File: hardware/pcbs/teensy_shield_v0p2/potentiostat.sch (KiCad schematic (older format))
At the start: 141 parts, among them K1 CONN_3, P1 CONN_2, P10 CONN_2, P11 CONN_2, P12 CONN_2, P13 CONN_5X2, P14 CONN_5X2, P15 CONN_2X2, P16 CONN_2X2, P17 CONN_2, P18 CONN_2, P19 CONN_2, P2 CONN_2, P20 CONN_2, P21 CONN_2, P3 CONN_2, P4 CONN_2, P5 CONN_2, P6 CONN_2, P7 CONN_2, P8 CONN_2, P9 CONN_2, U1 ZXRE060, U10 OPA227, U11 OP07, U12 LT1995, U13 ADG44X, U2 TEENSY3.1, U3 MAX6176AASA+, U4 LT1995, U5 AD8250, U6 MEA1D05XXSC, U7 OPA129, U8 OPA129, U9 ADG44X

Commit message: Worked on version 0.2 of teensy shield.
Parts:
- removed R?: 20k, symbol Device:R
- removed R? (x2): 10k, symbol Device:R
- removed R?: 50k, symbol Device:R
- removed R?: 120k, symbol Device:R
- removed R?: 36k, symbol Device:R
- removed U?: REF3312, symbol REF3312:REF3312
- added D?: BAS07-04, ~, symbol potentiostat-rescue:BAS07-04
- added R? (x2): 12k, symbol Device:R
- added R?: 100k, symbol Device:R
- added R? (x3): 20k, symbol Device:R
- added R?: 1k, symbol Device:R
- added R?: 100, symbol Device:R
- added U?: REF33XX, symbol REF33XX:REF33XX
- R?: value R -> 20k
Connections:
- net labels added: REF_3V, REF_NEG_0V6, REF_NEG_10V
- net labels removed: REF_1V25
- wire segments 702 -> 719
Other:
- note added: "-0.6V ref. voltage test point"
- note added: "3V Reference Voltage\n\nLCSC#: C140329\nREF3330AIDBZR"
- note added: "Notes:\n\n1.) Don't forget the bypass capacitors!!!\n2.) Maybe change +/-12V DC-DC converter to \n +/-15V DC-DC converter to give op07's more head room."
- note removed: "1.25V Reference Voltage\n\nLCSC#: C183104"
- note removed: "Don't forget the bypass capacitors!!!"
- note removed: "This will be inverting adder ...."
- moved on the sheet: C?, P10, P6, P7, P8, P9, R?, U?

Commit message: Worked on version 0.2 of teensy pcb.
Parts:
- added C? (x20): 0.1uF, symbol Device:C
- added C?: 3.3nF, symbol Device:C
- added C?: 12nF, symbol Device:C
- added C? (x4): 56nF, symbol Device:C
- added D?: BAS07-04, ~, symbol potentiostat-rescue:BAS07-04
- added K1: Conn_01x03, symbol Connector_Generic:Conn_01x03
- added P1, P2, P3: Conn_01x02, symbol Connector_Generic:Conn_01x02
- added R?: 300k, symbol Device:R
- added R?: 300, symbol Device:R
- added R?: 30k, symbol Device:R
- added R?: 3k, symbol Device:R
- added R? (x2): 20k, symbol Device:R
- added R? (x2): 12k, symbol Device:R
- added R?: 1k, symbol Device:R
- added R?: 100, symbol Device:R
- added R?: 10k, symbol Device:R
- added U? (x3): TL072, symbol Amplifier_Operational:TL072
- added U? (x15): DG411xY, Package_SO:SOIC-16_3.9x9.9mm_P1.27mm, symbol Analog_Switch:DG411xY
- added U?: 74HC138, symbol 74HC138:74HC138
- added U? (x2): OP07, symbol Amplifier_Operational:OP07
- U2: symbol potentiostat-rescue:TEENSY3.1 -> teensy3:TEENSY3.1
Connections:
- net labels added: CTR_ELECT_OUT, D3, D4, REF_ELECT_BIP, REF_ELECT_OUT, REF_GAIN_A0, REF_GAIN_A1, SW_CTR_ELECT, SW_REF_ELECT, SW_TIA_GAIN_1, SW_TIA_GAIN_2, SW_TIA_GAIN_3, SW_TIA_GAIN_4, SW_WRK_ELECT, TIA_GAIN_A0, TIA_GAIN_A1, WRK_ELECT_OUT
- net labels removed: DAC_GAIN_B0, DAC_GAIN_B1, REF_NEG_10V, RX, TX
- wire segments 719 -> 960
- no-connect marks 56 -> 68
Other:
- note added: "Notes:\n\n1.) Don't forget the bypass capacitors!!!\n2.) Maybe change DC converter from +/-12V to +/-15V \n3.) Add switch to working electrode ( and counter and reference?)\n4.) Add low pass filters to inputs (DAC) and outputs (ADC)\n"
- note added: "OP07\nLCSC# C7433"
- note added: "Scale bipolar DAC (DAC_BIP) by gain N=1,2,5, or 10 to get DAC_BIP_NX. \nGain is selected using DAC_GAIN_A0 and DAC_GAIN_A1"
- note added: "Shift and scales unipolar DAC (DAC_UNI) from [0V,1.2V] \nrange to bipolar DAC (DAC_BIP) in [-1V,1V] range. \n"
- note added: "TL072 power\n\nLCSC# C6961"
- note added: "gain select demux\nLCSC#: C5602"
- note added: "op amp decoupling capacitors"
- note added: "scale TIA signal by 2x"
- note added: "scale buffered reference electrode voltage\n according to gain setting"
- note added: "shift TIA signal to 0-1.2V range"
- note added: "switch power\nLCSC#: C17218"
- note added: "transimpedance amplifier with selectable gain using kelvin switching\nsee http://www.analog.com/library/analogdialogue/archives/47-05/pgtia.html\n\nSet gains so that output voltage range is -0.6V to 0.6V. \nInput current ranges (+/-) 1uA, 10uA, 100uA, 1000uA \n"
- note removed: "LCSC# C7433"
- note removed: "Notes:\n\n1.) Don't forget the bypass capacitors!!!\n2.) Maybe change +/-12V DC-DC converter to \n +/-15V DC-DC converter to give op07's more head room."
- moved on the sheet: C?, D?, K1, P1, P10, P2, P3, P6, P7, P8, P9, R?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

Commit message: Worked on revision 0.2 of teensy pcb.
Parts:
- removed C1, C30, C37, C39, C5: 10nF, ~, symbol potentiostat-rescue:C
- removed C10, C11, C12, C13, C14, C15, C17, C2, C23, C24, C25, C27, C28, C33, C34, C35, C6: 0.1uF, ~, symbol potentiostat-rescue:C
- removed C16, C18, C26, C29, C31, C36, C4, C8: 10uF, ~, symbol potentiostat-rescue:CP1
- removed C19, C20, C21, C22: 56nF, ~, symbol potentiostat-rescue:C
- removed C3, C32, C7: 4.7uF, ~, symbol potentiostat-rescue:CP1
- removed C38: 4.7uf, ~, symbol potentiostat-rescue:CP1
- removed C9: 1uF, ~, symbol potentiostat-rescue:C
- removed D1, D2: BAS07-04, ~, symbol potentiostat-rescue:BAS07-04
- removed K1: CONN_3, symbol potentiostat-rescue:CONN_3
- removed P1, P10, P11, P12, P17, P18, P19, P2, P20, P21, P3, P4, P5, P6, P7, P8, P9: CONN_2, symbol potentiostat-rescue:CONN_2
- removed P13, P14: CONN_5X2, symbol potentiostat-rescue:CONN_5X2
- removed P15, P16: CONN_2X2, symbol potentiostat-rescue:CONN_2X2
- removed R1, R15, R18: 1k, ~, symbol potentiostat-rescue:R
- removed R10, R11, R9: 50k, ~, symbol potentiostat-rescue:R
- removed R12, R13: 3k, ~, symbol potentiostat-rescue:R
- removed R14, R16: 4.7k, ~, symbol potentiostat-rescue:R
- removed R17, R19: 100, ~, symbol potentiostat-rescue:R
- removed R2, R3: 10k, ~, symbol potentiostat-rescue:R
- removed R4: 191, ~, symbol potentiostat-rescue:R
- removed R5: 600, ~, symbol potentiostat-rescue:R
- removed R6: 6k, ~, symbol potentiostat-rescue:R
- removed R7: 60k, ~, symbol potentiostat-rescue:R
- removed R8: 600k, ~, symbol potentiostat-rescue:R
- removed U1: ZXRE060, ~, symbol potentiostat-rescue:ZXRE060
- removed U10: OPA227, ~, symbol potentiostat-rescue:OPA227
- removed U11: OP07, ~, symbol potentiostat-rescue:OP07
- removed U12, U4: LT1995, ~, symbol potentiostat-rescue:LT1995
- removed U13, U9: ADG44X, symbol potentiostat-rescue:ADG44X
- removed U3: MAX6176AASA+, ~, symbol potentiostat-rescue:MAX6176AASA+
- removed U5: AD8250, ~, symbol potentiostat-rescue:AD8250
- removed U7, U8: OPA129, ~, symbol potentiostat-rescue:OPA129
- added C? (x16): 0.1uF, symbol Device:C
- added C? (x4): 1uF, symbol Device:C
- added C? (x3): 2.2uF, symbol Device:C
- added P10, P11, P12, P17, P18, P19, P20, P21, P4, P5, P6, P7, P8, P9, P?: Conn_01x02, symbol Connector_Generic:Conn_01x02
- added P13, P14: Conn_02x05_Odd_Even, symbol Connector_Generic:Conn_02x05_Odd_Even
- added P15, P16: Conn_02x02_Odd_Even, symbol Connector_Generic:Conn_02x02_Odd_Even
- added R? (x2): 4.7k, symbol Device:R
- U6: symbol potentiostat-rescue:MEA1D05XXSC -> mea1d05xxsc:MEA1D05XXSC
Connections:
- net labels removed: REF_10V, TIA_SW1_IN1, TIA_SW1_IN2, TIA_SW1_IN3, TIA_SW1_IN4, TIA_SW2_IN1, TIA_SW2_IN2, TIA_SW2_IN3, TIA_SW2_IN4
- wire segments 960 -> 650
- no-connect marks 68 -> 51
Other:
- note added: "0.6V reference test points"
- note added: "12V power decoupling caps"
- note added: "3V reference \n\nLCSC#: C140329\nREF3330AIDBZR"
- note added: "DAC test points"
- note added: "Reference electrode test points"
- note added: "TL072 power\nLCSC# C6961"
- note added: "bipolor/unipolar transimpedance \namplifier output test points"
- note added: "demux decoupling"
- note added: "demux decoupling capacitors"
- note added: "op amp decoupling"
- note added: "switch decoupling"
- note removed: "-0.6V ref. voltage test point"
- note removed: "0.6V ref. voltage test point"
- note removed: "10V Reference voltage."
- note removed: "10V ref. voltage test point"
- note removed: "3V Reference Voltage\n\nLCSC#: C140329\nREF3330AIDBZR"
- note removed: "Amplifier Gain=1.67"
- note removed: "DAC_GAIN_A0 and DAC_GAIN_A1."
- note removed: "Differential Amplifier - shifts and scales +/- 10V REF_ELECT_BUF into 0-1.2V range for analog input."
- note removed: "For switch arrangement see http://www.analog.com/library/analogdialogue/archives/47-05/pgtia.html\n\nSet gains so that output voltage range is -0.6V to 0.6V. \n\nInput current ranges (+/-) 1uA, 10uA, 100uA, 1000uA \n\nC values - may need tobe refined"
- note removed: "NX scaled DAC test point"
- note removed: "Scale bipolar DAC (DAC_BIP) by gain N=1,2,5, or 10 to get DAC_BIP_NX. Gain is selected using"
- note removed: "Shift and scales unipolar DAC (DAC_UNI) from [0V,1.2V] range to bipolar DAC (DAC_BIP) in [-1V,1V] range. \n"
- note removed: "TL072 power\n\nLCSC# C6961"
- note removed: "Transimpedance Amplifier"
- note removed: "Use ADG441"
- note removed: "Voltage Reference, 0.6V, Tol. 0.5%. Used in when shifting DAC_UNI to DAC_BIP."
- note removed: "bipolor/unipolar transimpedance \namplifier output test poinsts"
- note removed: "buffered ref. electrode test point"
- note removed: "op amp decoupling capacitors"
- note removed: "unipolar ref. electrode test point"
- note removed: "unipolar/bipolar DAC test points"
- moved on the sheet: C?, D?, R?, U2, U6, U?

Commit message: Finished initial draft of version 0.2 of teensy pcb.
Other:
- note added: "3V reference \nLCSC#: C140329\nREF3330AIDBZR"
- note added: "Analog Ouput Subsystem"
- note added: "Control & Reference Subsystem"
- note added: "Electrode Connection Subsystem"
- note added: "Expansion Headers"
- note added: "Op Amp Power Rails"
- note added: "Reference voltages"
- note added: "Switch and demux decoupling"
- note added: "Transimpedance Subsystem"
- note added: "electrode connections"
- note added: "inverts -0.6V reference to \ncreate 0.6V reference"
- note added: "power decoupling"
- note added: "scales 3V reference to \ncreate -0.6V reference"
- note added: "switches for connecting/disconnecting electrodes"
- note removed: "3V reference \n\nLCSC#: C140329\nREF3330AIDBZR"
- note removed: "Electrode Connectors"
- moved on the sheet: C?, D?, R?, U6, U?

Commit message: Worked on teensy shield version 0.2. Ported footprints from .mod to .kicad_mod.   Finished initial footprint assignments.
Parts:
- C1, C10, C11, C12, C13, C14, C15, C16, C17, C18, C19, C2, C20, C21, C22, C23, C24, C25, C26, C27, C28, C29, C3, C30, C31, C32, C33, C34, C35, C36, C37, C38, C39, C4, C40, C41, C42, C43, C44, C45, C46, C47, C48, C49, C5, C50, C51, C52, C6, C7, C8, C9: renamed from C?; footprint (none) -> Capacitor_SMD:C_0603_1608Metric
- D1, D2: renamed from D?; footprint ~ -> Package_TO_SOT_SMD:SOT-23
- K1: footprint (none) -> pin_array:PIN_ARRAY_3X1
- P1, P10, P11, P12, P17, P18, P19, P2, P20, P21, P3, P4, P5, P6, P7, P8, P9: footprint (none) -> pin_array:PIN_ARRAY_2X1
- P13, P14: footprint (none) -> 5x2_shrd_header:5X2_SHRD_HEADER
- P15, P16: footprint (none) -> pin_array:PIN_ARRAY_2X2
- P22: renamed from P?; footprint (none) -> pin_array:PIN_ARRAY_2X1
- R1, R10, R11, R12, R13, R14, R15, R16, R17, R18, R19, R2, R20, R21, R22, R23, R24, R25, R26, R27, R28, R29, R3, R30, R31, R32, R33, R34, R35, R36, R37, R38, R4, R5, R6, R7, R8, R9: renamed from R?; footprint (none) -> Resistor_SMD:R_0603_1608Metric
- U1, U19, U21: renamed from U?; footprint (none) -> Package_SO:SOIC-16_3.9x9.9mm_P1.27mm
- U10: renamed from U?; footprint (none) -> Package_TO_SOT_SMD:SOT-23
- U11, U12, U13, U14, U15, U16, U17, U18, U20, U9: renamed from U?; footprint (none) -> Package_SO:SOIC-8_3.9x4.9mm_P1.27mm
- U2: footprint ~ -> teensy3x:TEENSY3X
- U6: footprint ~ -> MEA1:MEA1
- gave numbers to parts that had none: 5
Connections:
- net labels added: +15V, -15V
- net labels removed: +12V, -12V
- wire segments 650 -> 652
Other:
- note added: "Notes:\n\n1.) Don't forget the bypass capacitors!!!\n2.) Maybe change DC converter from +/-15V to +/-15V \n3.) Add switch to working electrode ( and counter and reference?)\n4.) Add low pass filters to inputs (DAC) and outputs (ADC)\n"
- note removed: "Notes:\n\n1.) Don't forget the bypass capacitors!!!\n2.) Maybe change DC converter from +/-12V to +/-15V \n3.) Add switch to working electrode ( and counter and reference?)\n4.) Add low pass filters to inputs (DAC) and outputs (ADC)\n"

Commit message: Work on layout of teensy pcb version 0.2
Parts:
- added C53, C54, C55: 0.1uF, Capacitor_SMD:C_0603_1608Metric, symbol Device:C
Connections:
- wire segments 652 -> 658
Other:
- note added: "U18, U20 op amp decoupling"
- note added: "U9 op amp decoupling"
- moved on the sheet: C46, C49
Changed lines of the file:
@@
 Text Notes 8750 9275 0    60   ~ 0
 DAC test points
-Text Notes 26325 5800 0    60   ~ 0
+Text Notes 27500 5825 0    60   ~ 0
 bipolor/unipolar transimpedance \namplifier output test points
 Text Label 8200 11700 2    60   ~ 0
@@
 	27900 1325 27900 1475
 Text Notes 26575 2425 0    60   ~ 0
-op amp decoupling
+U18, U20 op amp decoupling
 $Comp
 L Device:C C34
@@
 	25575 1275 25575 1425
 Text Notes 24875 2425 0    60   ~ 0
-op amp decoupling
+U9 op amp decoupling
 $Comp
 L Device:C C10
@@
 L Device:C C46
 U 1 1 605E8CC1
-P 26950 3300
-F 0 "C46" H 27065 3346 50  0000 L CNN
-F 1 "0.1uF" H 27065 3255 50  0000 L CNN
-F 2 "Capacitor_SMD:C_0603_1608Metric" H 26988 3150 50  0001 C CNN
-F 3 "~" H 26950 3300 50  0001 C CNN
-	1    26950 3300
+P 25850 5150
+F 0 "C46" H 25965 5196 50  0000 L CNN
+F 1 "0.1uF" H 25965 5105 50  0000 L CNN
+F 2 "Capacitor_SMD:C_0603_1608Metric" H 25888 5000 50  0001 C CNN
+F 3 "~" H 25850 5150 50  0001 C CNN
+	1    25850 5150
 	1    0    0    -1
 $EndComp
@@
 L Device:C C49
 U 1 1 605E95B1
-P 27450 3300
-F 0 "C49" H 27565 3346 50  0000 L CNN
-F 1 "1uF" H 27565 3255 50  0000 L CNN
-F 2 "Capacitor_SMD:C_0603_1608Metric" H 27488 3150 50  0001 C CNN
-F 3 "~" H 27450 3300 50  0001 C CNN
-	1    27450 3300
+P 26350 5150
+F 0 "C49" H 26465 5196 50  0000 L CNN
+F 1 "1uF" H 26465 5105 50  0000 L CNN
+F 2 "Capacitor_SMD:C_0603_1608Metric" H 26388 5000 50  0001 C CNN
+F 3 "~" H 26350 5150 50  0001 C CNN
+	1    26350 5150
 	1    0    0    -1
 $EndComp
-Text Label 27450 3000 1    60   ~ 0
+Text Label 26350 4850 1    60   ~ 0
 3V3
-Text Label 26950 3000 1    60   ~ 0
+Text Label 25850 4850 1    60   ~ 0
 3V3
 Wire Wire Line
-	27450 3450 27450 3650
-Text Label 27450 3650 3    60   ~ 0
+	26350 5300 26350 5500
+Text Label 26350 5500 3    60   ~ 0
 GND
 Wire Wire Line
-	26950 3450 26950 3650
-Text Label 26950 3650 3    60   ~ 0
+	25850 5300 25850 5500
+Text Label 25850 5500 3    60   ~ 0
 GND
 Wire Wire Line
-	26950 3000 26950 3150
+	25850 4850 25850 5000
 Wire Wire Line
-	27450 3000 27450 3150
+	26350 4850 26350 5000
 $Comp
 L Device:C C13
@@
 Text Notes 24950 10925 0    60   ~ 0
 switch decoupling
-Text Notes 26775 4100 0    50   ~ 0
+Text Notes 25675 5950 0    50   ~ 0
 demux decoupling capacitors
 $Comp
@@
 Wire Wire Line
 	25525 3000 25525 3150
-Text Notes 25125 4100 0    60   ~ 0
+Text Notes 26175 4150 0    60   ~ 0
 switch decoupling
 $Comp
@@
 L Connector_Generic:Conn_01x02 P17
 U 1 1 67FDB608
-P 27400 4725
-F 0 "P17" H 27480 4717 50  0000 L CNN
-F 1 "Conn_01x02" H 27480 4626 50  0000 L CNN
-F 2 "pin_array:PIN_ARRAY_2X1" H 27400 4725 50  0001 C CNN
-F 3 "~" H 27400 4725 50  0001 C CNN
-	1    27400 4725
+P 28575 4750
+F 0 "P17" H 28655 4742 50  0000 L CNN
+F 1 "Conn_01x02" H 28655 4651 50  0000 L CNN
+F 2 "pin_array:PIN_ARRAY_2X1" H 28575 4750 50  0001 C CNN
+F 3 "~" H 28575 4750 50  0001 C CNN
+	1    28575 4750
 	1    0    0    -1
 $EndComp
@@
 L Connector_Generic:Conn_01x02 P18
 U 1 1 67FDF739
-P 27400 5325
-F 0 "P18" H 27480 5317 50  0000 L CNN
-F 1 "Conn_01x02" H 27480 5226 50  0000 L CNN
-F 2 "pin_array:PIN_ARRAY_2X1" H 27400 5325 50  0001 C CNN
-F 3 "~" H 27400 5325 50  0001 C CNN
-	1    27400 5325
+P 28575 5350
+F 0 "P18" H 28655 5342 50  0000 L CNN
+F 1 "Conn_01x02" H 28655 5251 50  0000 L CNN
+F 2 "pin_array:PIN_ARRAY_2X1" H 28575 5350 50  0001 C CNN
+F 3 "~" H 28575 5350 50  0001 C CNN
+	1    28575 5350
 	1    0    0    -1
 $EndComp
 Wire Wire Line
-	27200 4725 27100 4725
+	28375 4750 28275 4750
 Wire Wire Line
-	27100 4725 27100 4775
+	28275 4750 28275 4800
 Wire Wire Line
-	27100 4825 27200 4825
+	28275 4850 28375 4850
 Wire Wire Line
-	27200 5325 27100 5325
+	28375 5350 28275 5350
 Wire Wire Line
-	27100 5325 27100 5375
+	28275 5350 28275 5400
 Wire Wire Line
-	27100 5425 27200 5425
+	28275 5450 28375 5450
 Wire Wire Line
-	27100 4775 26850 4775
-Connection ~ 27100 4775
+	28275 4800 28025 4800
+Connection ~ 28275 4800
 Wire Wire Line
-	27100 4775 27100 4825
+	28275 4800 28275 4850
 Wire Wire Line
-	27100 5375 26850 5375
-Connection ~ 27100 5375
+	28275 5400 28025 5400
+Connection ~ 28275 5400
 Wire Wire Line
-	27100 5375 27100 5425
-Text Label 26850 5375 2    60   ~ 0
+	28275 5400 28275 5450
+Text Label 28025 5400 2    60   ~ 0
 TIA_OUT_UNI
-Text Label 26850 4775 2    60   ~ 0
+Text Label 28025 4800 2    60   ~ 0
 TIA_OUT_BIP
 $Comp
@@
 Wire Wire Line
 	3450 11300 3250 11300
+$Comp
+L Device:C C55
+U 1 1 603A4E43
+P 27925 3325
+F 0 "C55" H 28040 3371 50  0000 L CNN
+F 1 "0.1uF" H 28040 3280 50  0000 L CNN
+F 2 "Capacitor_SMD:C_0603_1608Metric" H 27963 3175 50  0001 C CNN
+F 3 "~" H 27925 3325 50  0001 C CNN
+	1    27925 3325
+	1    0    0    -1
+$EndComp
+Text Label 27925 3025 1    60   ~ 0
+3V3
+Wire Wire Line
+	27925 3475 27925 3675
+Text Label 27925 3675 3    60   ~ 0
+GND
+Wire Wire Line
+	27925 3025 27925 3175
+$Comp
+L Device:C C53
+U 1 1 603A5659
+P 26875 3325
+F 0 "C53" H 26990 3371 50  0000 L CNN
+F 1 "0.1uF" H 26990 3280 50  0000 L CNN
+F 2 "Capacitor_SMD:C_0603_1608Metric" H 26913 3175 50  0001 C CNN
+F 3 "~" H 26875 3325 50  0001 C CNN
+	1    26875 3325
+	1    0    0    -1
+$EndComp
+$Comp
+L Device:C C54
+U 1 1 603A5663
+P 27375 3325
+F 0 "C54" H 27490 3371 50  0000 L CNN
+F 1 "0.1uF" H 27490 3280 50  0000 L CNN
+F 2 "Capacitor_SMD:C_0603_1608Metric" H 27413 3175 50  0001 C CNN
+F 3 "~" H 27375 3325 50  0001 C CNN
+	1    27375 3325
+	1    0    0    -1
+$EndComp
+Text Label 26875 3025 1    60   ~ 0
+-15V
+Wire Wire Line
+	26875 3475 26875 3675
+Text Label 26875 3675 3    60   ~ 0
+AGND
+Wire Wire Line
+	27375 3475 27375 3675
+Text Label 27375 3675 3    60   ~ 0
+AGND
+Wire Wire Line
+	26875 3025 26875 3175
+Text Label 27375 3025 1    60   ~ 0
++15V
+Wire Wire Line
+	27375 3025 27375 3175
 $EndSCHEMATC

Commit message: Finished initial layout for version 0.2 of teensy pcb.
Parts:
- removed C49, C51: 1uF, Capacitor_SMD:C_0603_1608Metric, symbol Device:C
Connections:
- wire segments 658 -> 654
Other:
- note removed: "demux decoupling capacitors"
- moved on the sheet: C46
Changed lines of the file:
@@
 	1    0    0    -1
 $EndComp
-$Comp
-L Device:C C51
-U 1 1 604AA16D
-P 27500 10125
-F 0 "C51" H 27615 10171 50  0000 L CNN
-F 1 "1uF" H 27615 10080 50  0000 L CNN
-F 2 "Capacitor_SMD:C_0603_1608Metric" H 27538 9975 50  0001 C CNN
-F 3 "~" H 27500 10125 50  0001 C CNN
-	1    27500 10125
-	1    0    0    -1
-$EndComp
-Text Label 27500 9825 1    60   ~ 0
-3V3
 Text Label 27000 9825 1    60   ~ 0
 3V3
 Wire Wire Line
-	27500 10275 27500 10475
-Text Label 27500 10475 3    60   ~ 0
-GND
-Wire Wire Line
 	27000 10275 27000 10475
 Text Label 27000 10475 3    60   ~ 0
@@
 Wire Wire Line
 	27000 9825 27000 9975
-Wire Wire Line
-	27500 9825 27500 9975
 $Comp
 L Device:C C46
 U 1 1 605E8CC1
-P 25850 5150
-F 0 "C46" H 25965 5196 50  0000 L CNN
-F 1 "0.1uF" H 25965 5105 50  0000 L CNN
-F 2 "Capacitor_SMD:C_0603_1608Metric" H 25888 5000 50  0001 C CNN
-F 3 "~" H 25850 5150 50  0001 C CNN
-	1    25850 5150
-	1    0    0    -1
-$EndComp
-$Comp
-L Device:C C49
-U 1 1 605E95B1
-P 26350 5150
-F 0 "C49" H 26465 5196 50  0000 L CNN
-F 1 "1uF" H 26465 5105 50  0000 L CNN
-F 2 "Capacitor_SMD:C_0603_1608Metric" H 26388 5000 50  0001 C CNN
-F 3 "~" H 26350 5150 50  0001 C CNN
-	1    26350 5150
-	1    0    0    -1
-$EndComp
-Text Label 26350 4850 1    60   ~ 0
+P 26200 5150
+F 0 "C46" H 26315 5196 50  0000 L CNN
+F 1 "0.1uF" H 26315 5105 50  0000 L CNN
+F 2 "Capacitor_SMD:C_0603_1608Metric" H 26238 5000 50  0001 C CNN
+F 3 "~" H 26200 5150 50  0001 C CNN
+	1    26200 5150
+	1    0    0    -1
+$EndComp
+Text Label 26200 4850 1    60   ~ 0
 3V3
-Text Label 25850 4850 1    60   ~ 0
-3V3
-Wire Wire Line
-	26350 5300 26350 5500
-Text Label 26350 5500 3    60   ~ 0
-GND
-Wire Wire Line
-	25850 5300 25850 5500
-Text Label 25850 5500 3    60   ~ 0
-GND
-Wire Wire Line
-	25850 4850 25850 5000
-Wire Wire Line
-	26350 4850 26350 5000
+Wire Wire Line
+	26200 5300 26200 5500
+Text Label 26200 5500 3    60   ~ 0
+GND
+Wire Wire Line
+	26200 4850 26200 5000
 $Comp
 L Device:C C13
@@
 switch decoupling
 Text Notes 25675 5950 0    50   ~ 0
-demux decoupling capacitors
+demux decoupling
 $Comp
 L Device:C C41
@@
 F 0 "U2" H 2775 3375 60  0000 C CNN
 F 1 "TEENSY3.1" H 2775 375 60  0000 C CNN
-F 2 "teensy3x:TEENSY3X" H 2475 2225 60  0000 C CNN
+F 2 "teensy3x:TEENSY3X" H 3150 2025 60  0001 C CNN
 F 3 "~" H 2475 2225 60  0000 C CNN
 	1    2775 2025
@@
 Wire Wire Line
 	13050 16375 13050 16625
-Text Notes 26850 10925 0    60   ~ 0
+Text Notes 26650 10925 0    60   ~ 0
 demux decoupling
 $Comp

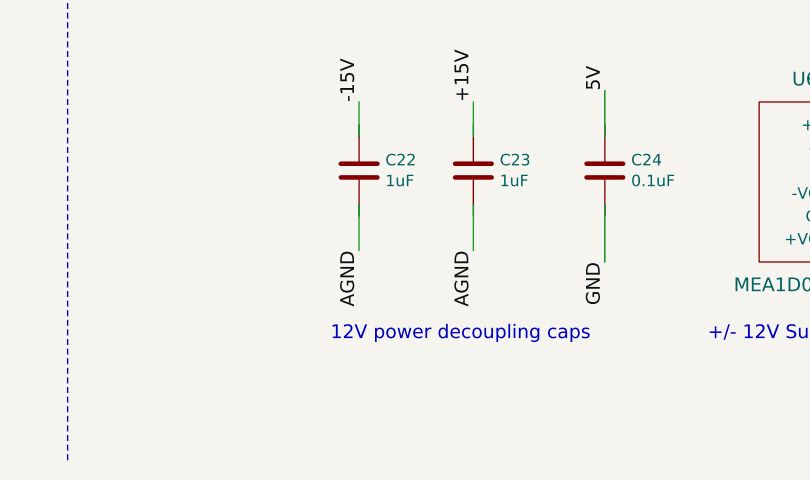
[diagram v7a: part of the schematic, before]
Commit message: Completed initial routing of PCB.
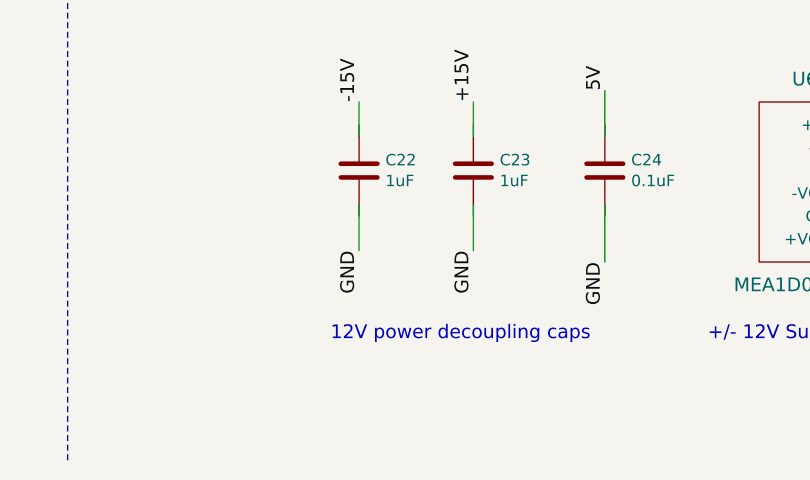
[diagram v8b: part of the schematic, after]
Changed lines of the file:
@@
 	11975 16375 11975 16575
 Text Label 11975 16575 3    60   ~ 0
-AGND
+GND
 Wire Wire Line
 	12475 16375 12475 16575
 Text Label 12475 16575 3    60   ~ 0
-AGND
+GND
 Wire Wire Line
 	11975 15925 11975 16075
